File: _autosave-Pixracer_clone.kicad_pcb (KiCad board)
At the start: 4 copper layers, 47.5 x 47.5 mm, 98 parts, among them J1 Conn_01x03_Male, J10 Conn_01x04_Male, J11 Conn_01x04_Male, J12 Conn_01x04_Male, J13 Conn_01x04_Male, J14 UART4_con, J15 UART4_con, J16 UART4_con, J17 Conn_01x06_Male, J18 Micro_SD_Card, J2 USB_B_Micro, J20 Conn_01x04_Male, J3 Conn_01x08_Male, J4 Conn_01x08_Male, J5 Conn_01x08_Male, J6 Conn_01x02_Male, J7 Conn_01x03_Male, J8 Conn_01x02_Male, J9 UART4_con, Q1 2N3904, Q2 2N3904, SW1 SW_Push, U1 STM32F427VITx, U10 LP5907MFX-3.3, U11 NRF24L01_Breakout, U2 USBLC6-2SC6, U3 ICM-20948, U4 MPU-9250, U5 LSM6DS3, U6 TJA1051T, U7 LP5907MFX-1.8, U8 LP5907MFX-3.3, U9 25LCxxx, Y1 Crystal_GND24

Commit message: a
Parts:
- C28, C29, C31, U7, U8: moved to F.Cu
- moved R6 34.5 mm to (155.5, 108.8), turned to 180 degrees
- moved R5 34.4 mm to (158.9, 108.8), turned to 180 degrees
- moved C31 22.4 mm to (176.5, 112.5), turned to 90 degrees
- moved U8 22.2 mm to (179.2, 112.6)
- moved C29 15.9 mm to (176.5, 116.7), turned to 90 degrees
- moved U7 15.8 mm to (179.1, 116.8)
- moved C28 15.8 mm to (181.7, 116.8), turned to 270 degrees
- moved D6 11.0 mm to (211.9, 83.3)
- moved R10 11.0 mm to (211.9, 84.8)
- moved C41 6.57 mm to (127.2, 80.5)
- moved C3 0.62 mm to (178.3, 107.6)
- moved R16 0.53 mm to (172.9, 80.4)
- moved U6 0.19 mm to (172.8, 84.4), turned to 90 degrees
- moved J20 0.06 mm to (173.3, 77.0)
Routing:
- net TIM1_CH4: track 7.71 -> 24.2 mm
- net TIM1_CH3: track 10.2 -> 24.7 mm
- net BOOT0: track 0.00 -> 5.66 mm
- net CAN1_RX: track 0.80 -> 5.41 mm
- net CAN1_TX: track 0.00 -> 2.87 mm
- net TIM1_CH1: track 20.2 -> 22.2 mm
- net +1V8: track 21.7 -> 22.9 mm

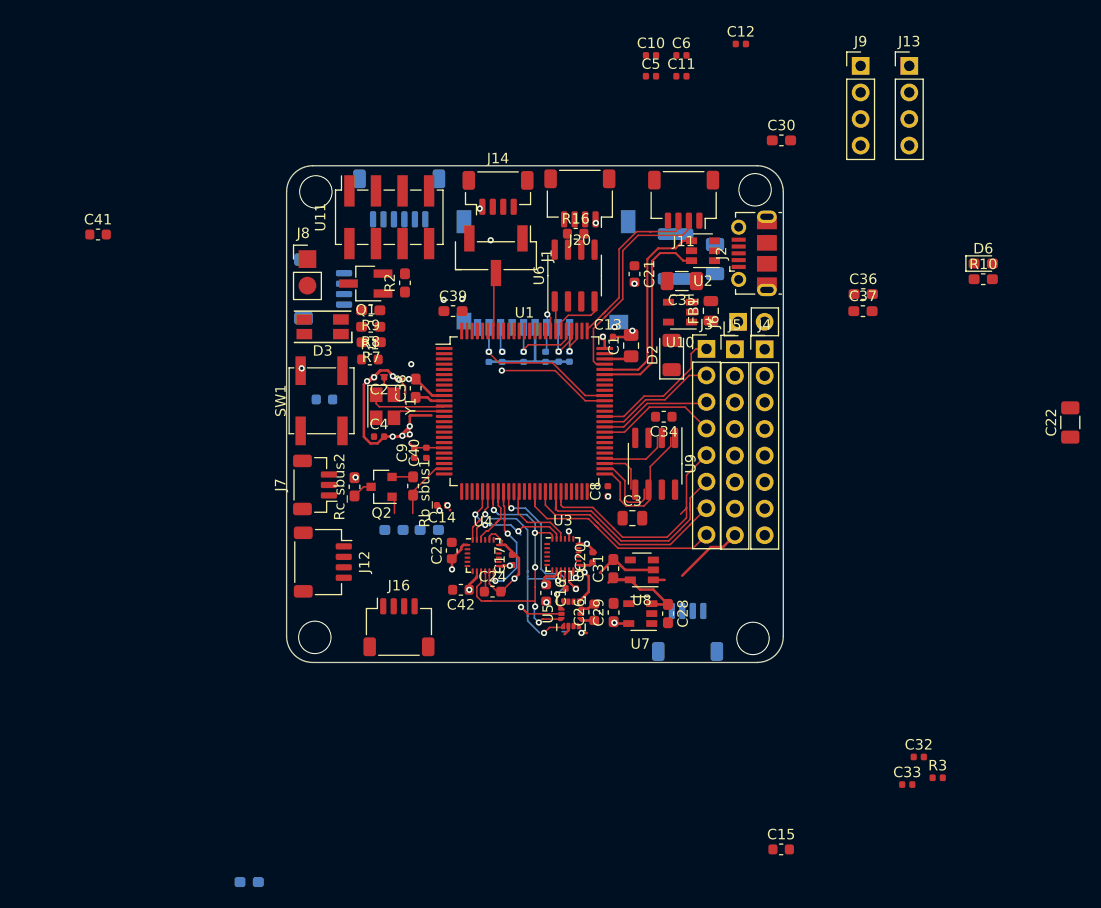
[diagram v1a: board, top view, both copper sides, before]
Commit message: add IMU external board
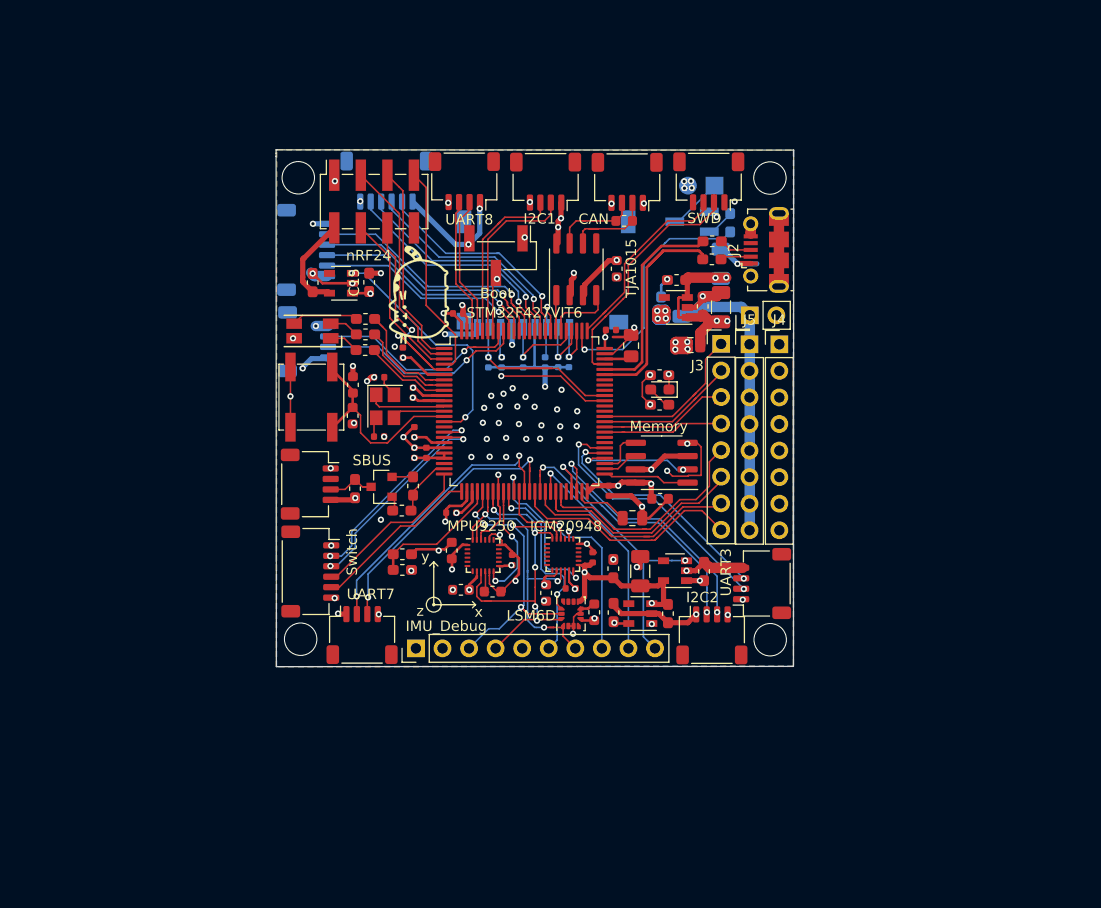
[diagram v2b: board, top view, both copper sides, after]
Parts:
- removed C11: 1u, Capacitor_SMD:C_0402_1005Metric
- removed C22: CP, Capacitor_SMD:C_1206_3216Metric
- removed C32: 1uF, Capacitor_SMD:C_0402_1005Metric
- removed C33: 100nF, Capacitor_SMD:C_0402_1005Metric
- removed C41: C, Capacitor_SMD:C_0603_1608Metric
- removed F1: Fuse, Fuse:Fuse_1812_4532Metric
- removed J11: Conn_01x04_Male, Connector_JST:JST_SH_SM04B-SRSS-TB_1x04-1MP_P1.00mm_Horizontal
- removed J13: Conn_01x04_Male, Connector_PinHeader_2.54mm:PinHeader_1x04_P2.54mm_Vertical
- removed J14: UART4_con, Connector_JST:JST_SH_BM04B-SRSS-TB_1x04-1MP_P1.00mm_Vertical
- removed J6: Conn_01x02_Male, Connector_PinHeader_2.54mm:PinHeader_1x02_P2.54mm_Vertical
- removed J7: Conn_01x03_Male, Connector_JST:JST_SH_BM03B-SRSS-TB_1x03-1MP_P1.00mm_Vertical
- removed J9: UART4_con, Connector_PinHeader_2.54mm:PinHeader_1x04_P2.54mm_Vertical
- added C25: CP, Capacitor_SMD:C_1206_3216Metric, F.Cu at (179.1, 112.7)
- added C43: 1uF, Capacitor_SMD:C_0603_1608Metric_Pad1.05x0.95mm_HandSolder, F.Cu at (147.8, 85.1)
- added G***: LOGO, pusheen:pusheen_small, F.Cu at (157.9, 86.3)
- added G***: LOGO, Pixracer_clone:pusheen, B.Cu at (166.4, 104.4)
- added I2C1: UART4_con, Connector_JST:JST_SH_SM04B-SRSS-TB_1x04-1MP_P1.00mm_Horizontal, F.Cu at (170.0, 75.5)
- added IMU_Debug: Conn_01x10_Male, Connector_PinHeader_2.54mm:PinHeader_1x10_P2.54mm_Vertical, F.Cu at (157.6, 120.1)
- added J19: Conn_01x02_Male, Connector_PinHeader_2.54mm:PinHeader_1x02_P2.54mm_Vertical, F.Cu at (189.6, 88.2)
- added R4: 22R, Resistor_SMD:R_0603_1608Metric_Pad1.05x0.95mm_HandSolder, F.Cu at (185.9, 82.9)
- added SBUS: Conn_01x04_Male, Connector_JST:JST_SH_SM04B-SRSS-TB_1x04-1MP_P1.00mm_Horizontal, F.Cu at (147.5, 104.4)
- added SPI3: Conn_01x06_Male, Connector_JST:JST_SH_SM06B-SRSS-TB_1x06-1MP_P1.00mm_Horizontal, B.Cu at (147.1, 82.0)
- added SWD: Conn_01x04_Male, Connector_JST:JST_SH_SM04B-SRSS-TB_1x04-1MP_P1.00mm_Horizontal, F.Cu at (185.6, 75.4)
- added Switch: Conn_01x06_Male, Connector_JST:JST_SH_SM06B-SRSS-TB_1x06-1MP_P1.00mm_Horizontal, F.Cu at (147.5, 112.7)
- added UART8: Conn_01x04_Male, Connector_JST:JST_SH_SM04B-SRSS-TB_1x04-1MP_P1.00mm_Horizontal, F.Cu at (162.2, 75.4)
- added x: indicator, Pixracer_clone:indicator, F.Cu at (159.3, 115.9)
- Buzzer: renamed from J8; moved to B.Cu
- C15: value C -> 1uF; footprint Capacitor_SMD:C_0603_1608Metric -> Capacitor_SMD:C_0603_1608Metric_Pad1.05x0.95mm_HandSolder
- C39, D2, Q1, R2: moved to B.Cu
- C7, R5, R6, Rc_sbus1: moved to F.Cu
- I2C2: renamed from J15; moved to F.Cu
- R3: value R -> 22R; footprint Resistor_SMD:R_0402_1005Metric -> Resistor_SMD:R_0603_1608Metric_Pad1.05x0.95mm_HandSolder
- U2: value USBLC6-2SC6 -> LP5907MFX-3.3; footprint Package_TO_SOT_SMD:SOT-23-6 -> Package_TO_SOT_SMD:SOT-23-5
- moved C15 67.0 mm to (153.2, 85.1), turned to 90 degrees
- moved R3 55.7 mm to (185.9, 81.2), turned to 180 degrees
- moved C12 48.5 mm to (157.5, 99.4), turned to 90 degrees
- moved C30 41.9 mm to (185.2, 112.7), turned to 90 degrees
- moved Buzzer 39.6 mm to (186.2, 75.8), turned to 90 degrees
- moved C10 39.5 mm to (157.3, 95.6), turned to 90 degrees
- moved C6 39.0 mm to (156.4, 91.8), turned to 90 degrees
- moved Rc_sbus1 38.4 mm to (156.3, 106.9)
- moved UART3 35.0 mm to (190.7, 113.9), turned to 90 degrees
- moved U2 34.8 mm to (150.5, 85.2)
- moved R10 33.2 mm to (180.9, 96.8)
- moved D6 33.2 mm to (180.9, 95.3), turned to 180 degrees
- moved Q1 31.8 mm to (184.0, 79.3)
- moved R2 31.6 mm to (187.7, 79.4)
- moved C5 29.2 mm to (161.7, 88.0)
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- renumbered J1 to Boot, J20 to CAN, U3 to ICM20948, U5 to LSM6D, U4 to MPU9250, U9 to Memory, J18 to SDcard, U1 to STM32F427VIT6, U6 to TJA1015, J17 to Telemetry, J10 to UART1, J16 to UART3, J12 to UART7, U11 to nRF24
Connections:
- Buzzer pad 2: 5V_IN -> +5V
- C15 pad 1: VBUS -> +5V
- C21 pad 1: 5V_IN -> +5V
- C30 pad 1: 5V_IN -> +5V
- CAN pad 4: 5V_IN -> +5V
- D2 pad 1: 5V_IN -> +5V
- I2C2 pad 2: I2C2_SDA -> I2C2_SCl
- I2C2 pad 3: I2C2_SCl -> I2C2_SDA
- I2C2 pad 4: 5V_IN -> +5V
- J5 pad 1: 5V_IN -> +5V
- J5 pad 2: 5V_IN -> +5V
- J5 pad 3: 5V_IN -> +5V
- J5 pad 4: 5V_IN -> +5V
- J5 pad 5: 5V_IN -> +5V
- J5 pad 6: 5V_IN -> +5V
- J5 pad 7: 5V_IN -> +5V
- J5 pad 8: 5V_IN -> +5V
- R3 pad 1: +3.3VA -> /USB_sheet/D+
- R3 pad 2: ICM20948_CS -> USB_D+
- R5 pad 1: 5V_IN -> +5V
- Rc_sbus2 pad 2: 5V_IN -> +5V
- STM32F427VIT6 pad 3: SPI4_MOSI -> SPI4_CS
- STM32F427VIT6 pad 43: Net-(U1-Pad43) -> EXTERNAL_MPU_CS
- STM32F427VIT6 pad 51: Net-(U1-Pad51) -> EXTERNAL_MEM_CS
- STM32F427VIT6 pad 57: EXTERNAL_MEM_CS -> Net-(U1-Pad57)
- TJA1015 pad 3: 5V_IN -> +5V
- Telemetry pad 1: VCC -> +5V
- U2 pad 1: /USB_sheet/D- -> +5V
- U2 pad 3: /USB_sheet/D+ -> nRF24_EN
- U2 pad 4: USB_D+ -> Net-(U2-Pad4)
- U2 pad 5: VBUS -> Net-(C43-Pad1)
- U8 pad 1: 5V_IN -> +5V
- UART1 pad 2: UART1_RX -> UART1_TX
- UART1 pad 3: UART1_TX -> UART1_RX
- UART1 pad 4: VCC -> +5V
- UART3 pad 1: VCC -> +5V
- UART7 pad 4: VCC -> +5V
- nRF24 pad 1: Net-(U11-Pad1) -> GND
- nRF24 pad 2: Net-(U11-Pad2) -> Net-(C43-Pad1)
- nRF24 pad 3: Net-(U11-Pad3) -> SPI4_CE
- nRF24 pad 4: Net-(U11-Pad4) -> SPI4_CS
- nRF24 pad 5: Net-(U11-Pad5) -> SPI4_CLK
- nRF24 pad 6: Net-(U11-Pad6) -> SPI4_MOSI
- nRF24 pad 7: Net-(U11-Pad7) -> SPI4_MISO
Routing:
- net +5V: track 0.00 -> 215.8 mm, vias 0 -> 19
- net VCC: track 15.1 -> 156.1 mm, vias 4 -> 19
- net GND: track 72.7 -> 140.7 mm, vias 24 -> 77
- net 3.3_SENSE_EN: track 0.00 -> 30.0 mm, vias 0 -> 2
- net UART7_RX: track 0.00 -> 27.7 mm, vias 0 -> 2
- net UART7_TX: track 0.00 -> 27.4 mm, vias 0 -> 2
- net I2C2_SCl: track 0.00 -> 26.2 mm, vias 0 -> 2
- net UART3_TX: track 0.00 -> 26.2 mm, vias 0 -> 2
- net I2C2_SDA: track 0.00 -> 25.0 mm, vias 0 -> 2
- net SPI3_CS: track 0.00 -> 24.3 mm, vias 0 -> 1
- net Buzzer: track 0.00 -> 24.1 mm, vias 0 -> 1
- net nRF24_EN: track 0.00 -> 23.5 mm, vias 0 -> 2
- net SPI3_SCK: track 0.00 -> 23.1 mm, vias 0 -> 1
- net SPI4_MOSI: track 0.00 -> 23.0 mm, vias 0 -> 2
- net UART3_RX: track 0.00 -> 23.0 mm, vias 0 -> 2
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- added copper zone on B.Cu, net GND
- added copper zone on F.Cu, net GND
- added copper zone on In1.Cu, net GND
- added copper zone on In2.Cu, net VCC
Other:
- board size 47.5 x 47.5 mm -> 49.5 x 49.4 mm
- net class Default removed
- net class OSC removed
